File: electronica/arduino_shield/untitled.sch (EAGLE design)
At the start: 16 parts

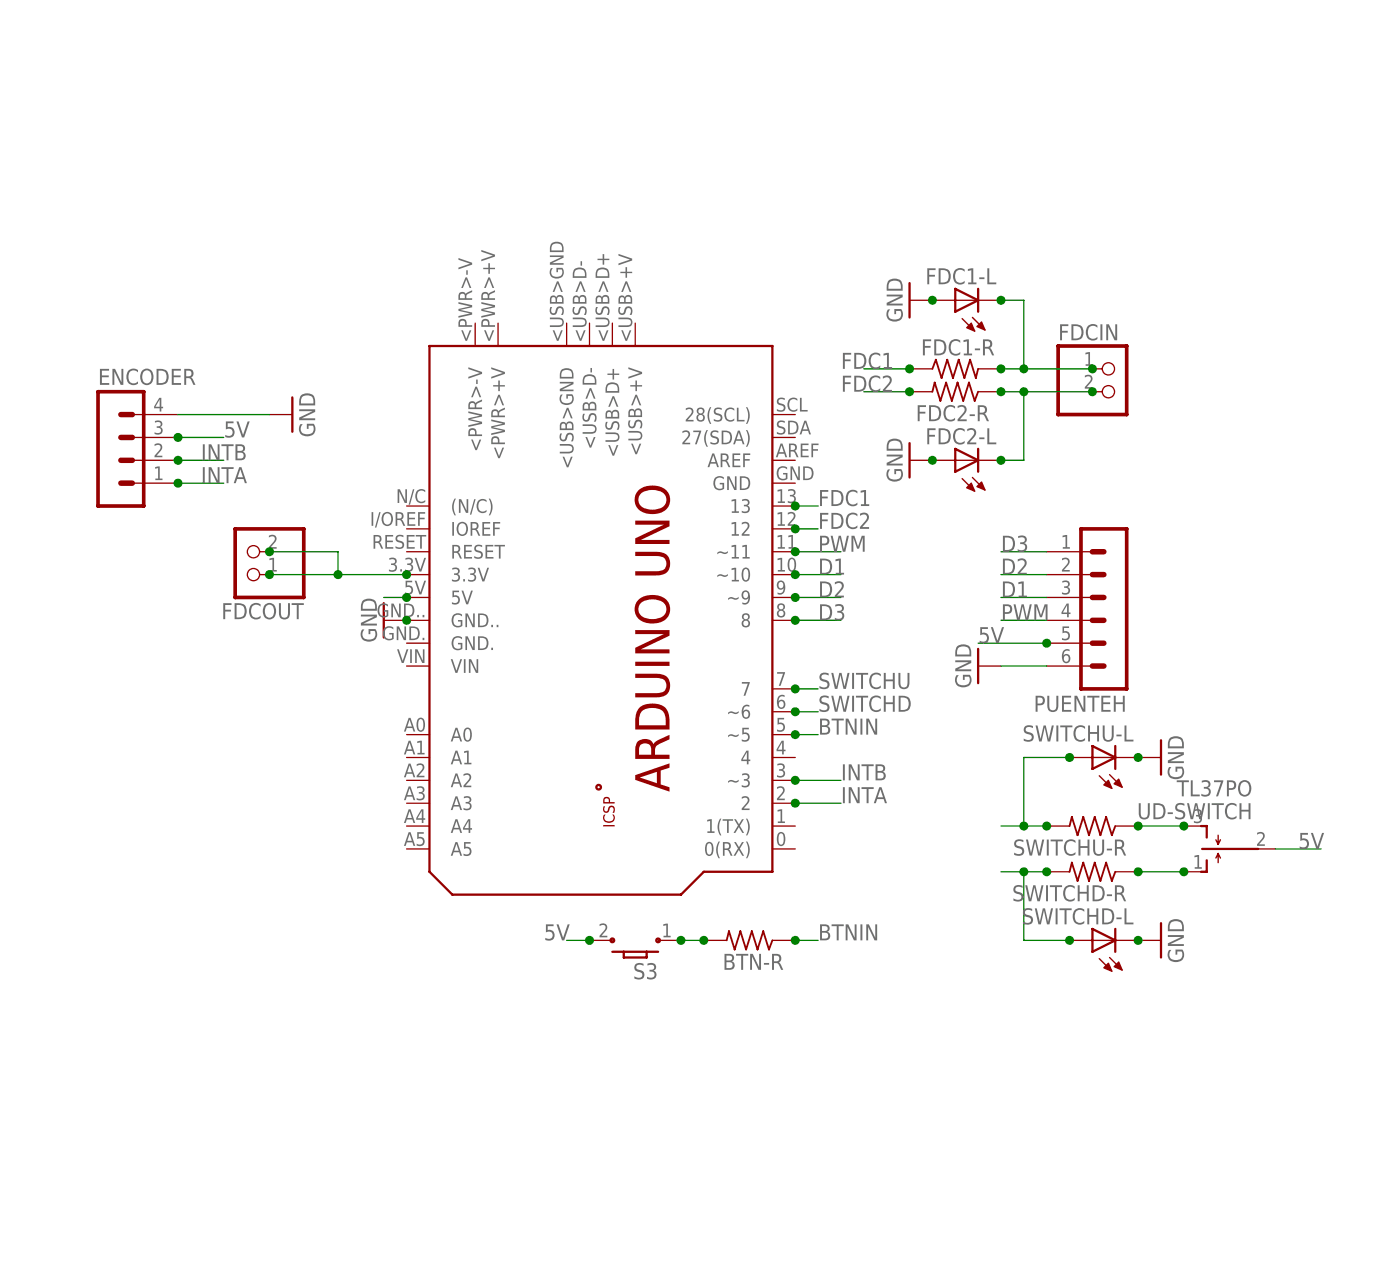
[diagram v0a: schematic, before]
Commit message: shield arduino terminado
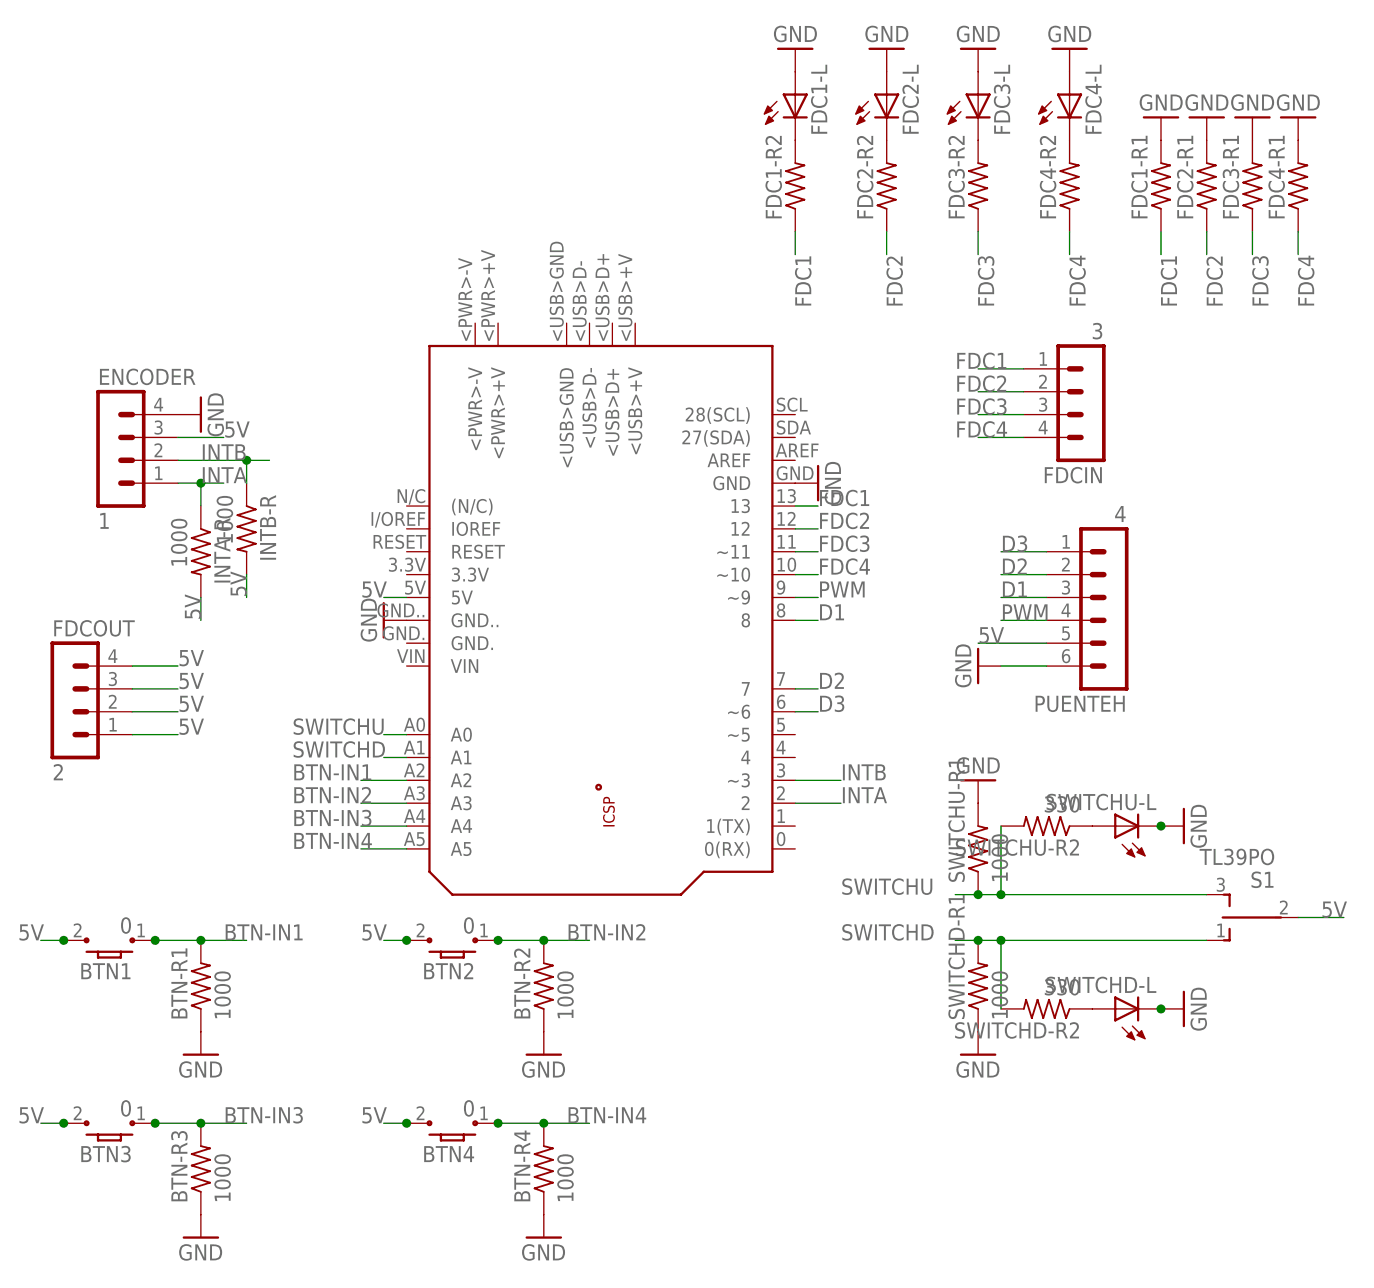
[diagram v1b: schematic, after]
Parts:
- removed BTN-R, FDC1-R, FDC2-R, SWITCHD-R, SWITCHU-R: (no value), resistor:R-US_0204/7
- removed S3: (no value), eswitch-tact:TL3302-J
- removed UD-SWITCH: TL37PO, switch:TL37PO
- added BTN-R1, BTN-R2, BTN-R3, BTN-R4, INTA-R, INTB-R, SWITCHD-R1, SWITCHU-R1: 1000, resistor:R-US_0204/7
- added BTN1, BTN2, BTN3, BTN4: 0, eswitch-tact:TL3302-J
- added FDC1-R1, FDC1-R2, FDC2-R1, FDC2-R2, FDC3-R1, FDC3-R2, FDC4-R1, FDC4-R2: (no value), resistor:R-US_0204/7
- added FDC3-L, FDC4-L: (no value), eagle-ltspice:LED_ELD260
- added S1: TL39PO, switch:TL39PO
- added SWITCHD-R2, SWITCHU-R2: 330, resistor:R-US_0204/7
- ENCODER: value (none) -> 1
- FDC1-L, FDC2-L, SWITCHD-L, SWITCHU-L: device eagle-ltspice:LED_ESML0603 -> eagle-ltspice:LED_ELD260
- FDCIN: value (none) -> 3; device pinhead:PINHD-1X2/90 -> con-lstb:MA04-1
- FDCOUT: value (none) -> 2; device pinhead:PINHD-1X2/90 -> con-lstb:MA04-1
- PUENTEH: value (none) -> 4
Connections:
- removed net 3.3V: FDCOUT.1, FDCOUT.2, PCB1.3.3V
- removed net BTNIN: BTN-R.1, PCB1.~5
- removed net N$5: BTN-R.2, S3.1
- new net BTN-IN1: BTN-R1.2, BTN1.1, PCB1.A2
- new net BTN-IN2: BTN-R2.2, BTN2.1, PCB1.A3
- new net BTN-IN3: BTN-R3.2, BTN3.1, PCB1.A4
- new net BTN-IN4: BTN-R4.2, BTN4.1, PCB1.A5
- new net FDC3: FDC3-R1.1, FDC3-R2.1, FDCIN.3, PCB1.~11
- new net FDC4: FDC4-R1.1, FDC4-R2.1, FDCIN.4, PCB1.~10
- new net N$6: FDC3-L.C, FDC3-R2.2
- new net N$7: FDC4-L.C, FDC4-R2.2
- net 5V: now also BTN1.2, BTN2.2, BTN3.2, BTN4.2, FDCOUT.1, FDCOUT.2, FDCOUT.3, FDCOUT.4, INTA-R.2, INTB-R.2, S1.P; no longer S3.2, UD-SWITCH.P
- net D1: now also PCB1.8; no longer PCB1.~10
- net D2: now also PCB1.7; no longer PCB1.~9
- net D3: now also PCB1.~6; no longer PCB1.8
- net FDC1: now also FDC1-R1.1, FDC1-R2.1, FDCIN.1; no longer FDC1-R.1
- net FDC2: now also FDC2-R1.1, FDC2-R2.1, FDCIN.2; no longer FDC2-R.2
- net GND: now also BTN-R1.1, BTN-R2.1, BTN-R3.1, BTN-R4.1, FDC1-R1.2, FDC2-R1.2, FDC3-L.A, FDC3-R1.2, FDC4-L.A, FDC4-R1.2, PCB1.GND, SWITCHD-R1.1, SWITCHU-R1.2
- net INTA: now also INTA-R.1
- net INTB: now also INTB-R.1
- net N$1: now also FDC1-R2.2; no longer FDC1-R.2, FDCIN.1
- net N$2: now also FDC2-R2.2; no longer FDC2-R.1, FDCIN.2
- net N$3: now also SWITCHU-L.A, SWITCHU-R2.1; no longer SWITCHU-R.1, UD-SWITCH.S
- net N$4: now also SWITCHD-L.A, SWITCHD-R2.1; no longer SWITCHD-R.1, UD-SWITCH.O
- net PWM: now also PCB1.~9; no longer PCB1.~11
- net SWITCHD: now also PCB1.A1, S1.O, SWITCHD-R1.2, SWITCHD-R2.2; no longer PCB1.~6, SWITCHD-L.A, SWITCHD-R.2
- net SWITCHU: now also PCB1.A0, S1.S, SWITCHU-R1.1, SWITCHU-R2.2; no longer PCB1.7, SWITCHU-L.A, SWITCHU-R.2
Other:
- moved on the sheet: FDC1-L, FDC2-L, SWITCHD-L, SWITCHU-L

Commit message: correccion de planos, adicion de potenciometro
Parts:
- added R1: PC16S, piher:PC16S
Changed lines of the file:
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@@
 <grid distance="0.1" unitdist="inch" unit="inch" style="lines" multiple="1" display="no" altdistance="0.01" altunitdist="inch" altunit="inch"/>
 <layers>
-<layer number="1" name="Top" color="4" fill="1" visible="yes" active="no"/>
-<layer number="2" name="Route2" color="1" fill="3" visible="yes" active="no"/>
-<layer number="3" name="Route3" color="4" fill="3" visible="yes" active="no"/>
-<layer number="4" name="Route4" color="1" fill="4" visible="yes" active="no"/>
-<layer number="5" name="Route5" color="4" fill="4" visible="yes" active="no"/>
-<layer number="6" name="Route6" color="1" fill="8" visible="yes" active="no"/>
-<layer number="7" name="Route7" color="4" fill="8" visible="yes" active="no"/>
-<layer number="8" name="Route8" color="1" fill="2" visible="yes" active="no"/>
-<layer number="9" name="Route9" color="4" fill="2" visible="yes" active="no"/>
-<layer number="10" name="Route10" color="1" fill="7" visible="yes" active="no"/>
-<layer number="11" name="Route11" color="4" fill="7" visible="yes" active="no"/>
-<layer number="12" name="Route12" color="1" fill="5" visible="yes" active="no"/>
-<layer number="13" name="Route13" color="4" fill="5" visible="yes" active="no"/>
-<layer number="14" name="Route14" color="1" fill="6" visible="yes" active="no"/>
-<layer number="15" name="Route15" color="4" fill="6" visible="yes" active="no"/>
-<layer number="16" name="Bottom" color="1" fill="1" visible="yes" active="no"/>
-<layer number="17" name="Pads" color="2" fill="1" visible="yes" active="no"/>
-<layer number="18" name="Vias" color="2" fill="1" visible="yes" active="no"/>
-<layer number="19" name="Unrouted" color="6" fill="1" visible="yes" active="no"/>
-<layer number="20" name="Dimension" color="15" fill="1" visible="yes" active="no"/>
-<layer number="21" name="tPlace" color="7" fill="1" visible="yes" active="no"/>
-<layer number="22" name="bPlace" color="7" fill="1" visible="yes" active="no"/>
-<layer number="23" name="tOrigins" color="15" fill="1" visible="yes" active="no"/>
-<layer number="24" name="bOrigins" color="15" fill="1" visible="yes" active="no"/>
-<layer number="25" name="tNames" color="7" fill="1" visible="yes" active="no"/>
-<layer number="26" name="bNames" color="7" fill="1" visible="yes" active="no"/>
-<layer number="27" name="tValues" color="7" fill="1" visible="yes" active="no"/>
-<layer number="28" name="bValues" color="7" fill="1" visible="yes" active="no"/>
+<layer number="1" name="Top" color="4" fill="1" visible="no" active="no"/>
+<layer number="2" name="Route2" color="1" fill="3" visible="no" active="no"/>
+<layer number="3" name="Route3" color="4" fill="3" visible="no" active="no"/>
+<layer number="4" name="Route4" color="1" fill="4" visible="no" active="no"/>
+<layer number="5" name="Route5" color="4" fill="4" visible="no" active="no"/>
+<layer number="6" name="Route6" color="1" fill="8" visible="no" active="no"/>
+<layer number="7" name="Route7" color="4" fill="8" visible="no" active="no"/>
+<layer number="8" name="Route8" color="1" fill="2" visible="no" active="no"/>
+<layer number="9" name="Route9" color="4" fill="2" visible="no" active="no"/>
+<layer number="10" name="Route10" color="1" fill="7" visible="no" active="no"/>
+<layer number="11" name="Route11" color="4" fill="7" visible="no" active="no"/>
+<layer number="12" name="Route12" color="1" fill="5" visible="no" active="no"/>
+<layer number="13" name="Route13" color="4" fill="5" visible="no" active="no"/>
+<layer number="14" name="Route14" color="1" fill="6" visible="no" active="no"/>
+<layer number="15" name="Route15" color="4" fill="6" visible="no" active="no"/>
+<layer number="16" name="Bottom" color="1" fill="1" visible="no" active="no"/>
+<layer number="17" name="Pads" color="2" fill="1" visible="no" active="no"/>
+<layer number="18" name="Vias" color="2" fill="1" visible="no" active="no"/>
+<layer number="19" name="Unrouted" color="6" fill="1" visible="no" active="no"/>
+<layer number="20" name="Dimension" color="15" fill="1" visible="no" active="no"/>
+<layer number="21" name="tPlace" color="7" fill="1" visible="no" active="no"/>
+<layer number="22" name="bPlace" color="7" fill="1" visible="no" active="no"/>
+<layer number="23" name="tOrigins" color="15" fill="1" visible="no" active="no"/>
+<layer number="24" name="bOrigins" color="15" fill="1" visible="no" active="no"/>
+<layer number="25" name="tNames" color="7" fill="1" visible="no" active="no"/>
+<layer number="26" name="bNames" color="7" fill="1" visible="no" active="no"/>
+<layer number="27" name="tValues" color="7" fill="1" visible="no" active="no"/>
+<layer number="28" name="bValues" color="7" fill="1" visible="no" active="no"/>
 <layer number="29" name="tStop" color="7" fill="3" visible="no" active="no"/>
 <layer number="30" name="bStop" color="7" fill="6" visible="no" active="no"/>
@@
 <layer number="35" name="tGlue" color="7" fill="4" visible="no" active="no"/>
 <layer number="36" name="bGlue" color="7" fill="5" visible="no" active="no"/>
-<layer number="37" name="tTest" color="7" fill="1" visible="yes" active="no"/>
-<layer number="38" name="bTest" color="7" fill="1" visible="yes" active="no"/>
+<layer number="37" name="tTest" color="7" fill="1" visible="no" active="no"/>
+<layer number="38" name="bTest" color="7" fill="1" visible="no" active="no"/>
 <layer number="39" name="tKeepout" color="4" fill="11" visible="no" active="no"/>
 <layer number="40" name="bKeepout" color="1" fill="11" visible="no" active="no"/>
@@
 <layer number="44" name="Drills" color="7" fill="1" visible="no" active="no"/>
 <layer number="45" name="Holes" color="7" fill="1" visible="no" active="no"/>
-<layer number="46" name="Milling" color="3" fill="1" visible="yes" active="no"/>
-<layer number="47" name="Measures" color="7" fill="1" visible="yes" active="no"/>
-<layer number="48" name="Document" color="7" fill="1" visible="yes" active="no"/>
-<layer number="49" name="Reference" color="7" fill="1" visible="yes" active="no"/>
-<layer number="50" name="dxf" color="7" fill="1" visible="yes" active="no"/>
-<layer number="51" name="tDocu" color="7" fill="1" visible="yes" active="no"/>
-<layer number="52" name="bDocu" color="7" fill="1" visible="yes" active="no"/>
-<layer number="53" name="tGND_GNDA" color="7" fill="9" visible="yes" active="no"/>
-<layer number="54" name="bGND_GNDA" color="1" fill="9" visible="yes" active="no"/>
-<layer number="56" name="wert" color="7" fill="1" visible="yes" active="no"/>
+<layer number="46" name="Milling" color="3" fill="1" visible="no" active="no"/>
+<layer number="47" name="Measures" color="7" fill="1" visible="no" active="no"/>
+<layer number="48" name="Document" color="7" fill="1" visible="no" active="no"/>
+<layer number="49" name="Reference" color="7" fill="1" visible="no" active="no"/>
+<layer number="50" name="dxf" color="7" fill="1" visible="no" active="no"/>
+<layer number="51" name="tDocu" color="7" fill="1" visible="no" active="no"/>
+<layer number="52" name="bDocu" color="7" fill="1" visible="no" active="no"/>
+<layer number="53" name="tGND_GNDA" color="7" fill="9" visible="no" active="no"/>
+<layer number="54" name="bGND_GNDA" color="1" fill="9" visible="no" active="no"/>
+<layer number="56" name="wert" color="7" fill="1" visible="no" active="no"/>
 <layer number="90" name="Modules" color="5" fill="1" visible="yes" active="yes"/>
 <layer number="91" name="Nets" color="2" fill="1" visible="yes" active="yes"/>
@@
 <part name="GND14" library="supply1" deviceset="GND" device=""/>
 <part name="GND18" library="supply1" deviceset="GND" device=""/>
+<part name="R1" library="piher" deviceset="PC16S" device=""/>
 </parts>
 <sheets>
@@
 <instance part="GND14" gate="1" x="20.32" y="15.24"/>
 <instance part="GND18" gate="1" x="20.32" y="-5.08"/>
+<instance part="R1" gate="G$1" x="88.9" y="15.24"/>
 </instances>
 <busses>
